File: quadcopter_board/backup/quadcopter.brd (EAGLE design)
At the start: 115.2 x 115.3 mm, 75 parts, among them J2 AVR_SPI_PRG_6NS, SW1 PUSHBUTTON_SMD-VERTICAL-1, U2 ATMEGA128RFA1

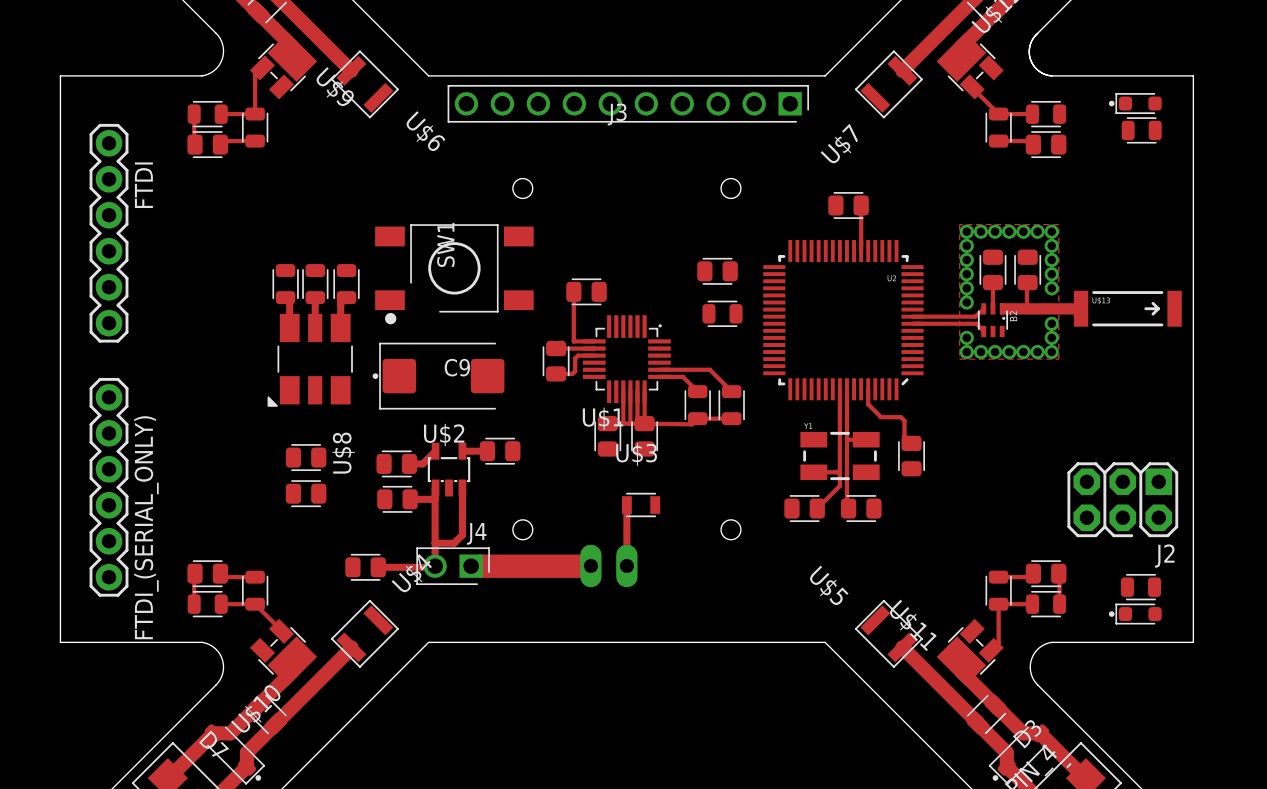
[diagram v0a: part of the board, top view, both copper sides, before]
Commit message: POURED SHIELDING FOR ANT
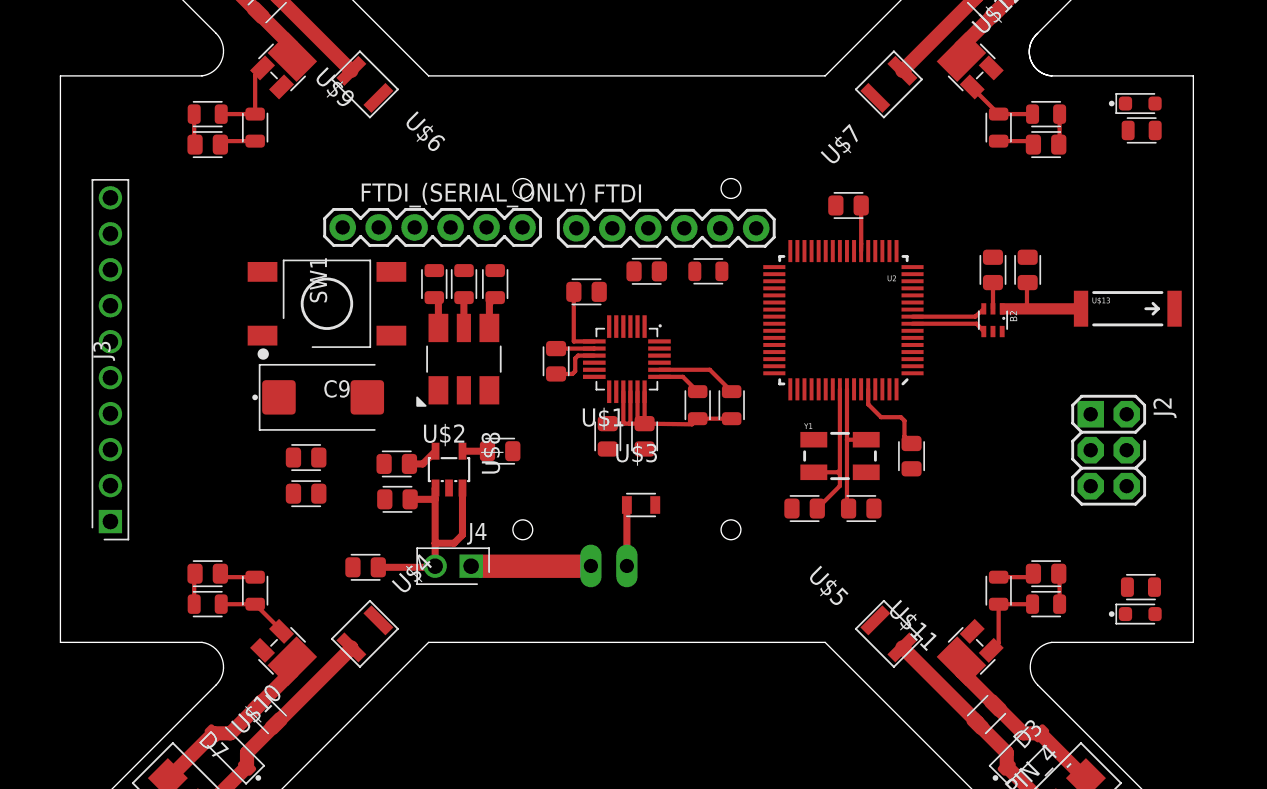
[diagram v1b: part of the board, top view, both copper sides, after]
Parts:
- moved J3 56.3 mm to (-36.5, -11.5), turned to 90 degrees
- moved FTDI 33.5 mm to (-3.57, 9.24), turned to 0 degrees
- moved FTDI_(SERIAL_ONLY) 20.4 mm to (-20.1, 9.30), turned to 0 degrees
- moved R16 10.5 mm to (-13.6, 5.30)
- moved U$8 10.5 mm to (-11.5, 0.00)
- moved R14 10.5 mm to (-9.30, 5.30)
- moved R15 10.5 mm to (-11.5, 5.30)
- moved SW1 9.34 mm to (-21.2, 3.91)
- moved C9 8.63 mm to (-21.4, -2.70)
- moved C3 5.00 mm to (1.40, 6.20)
- moved J2 3.64 mm to (34.0, -6.43), turned to 270 degrees
- moved R5 3.16 mm to (5.75, 6.20)
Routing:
- net BAT_GND: track 10.8 -> 13.0 mm
- removed copper zone on layer 1, net GND
- removed copper zone on layer 2, net GND
- removed copper zone on layer 2, net N$10
- removed copper zone on layer 15, net N$11
